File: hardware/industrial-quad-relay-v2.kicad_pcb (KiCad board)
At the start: 2 copper layers, 40 x 40 mm, 36 parts, among them P1 CON-SENSOR, P2 Digital Output, P3 Debug, P4 Boot, U1 XMC1100, U2 CPC1020N, U3 CPC1020N, U4 CPC1020N, U5 CPC1020N, U6 DRILL, U7 DRILL, U8 DRILL, U9 DRILL

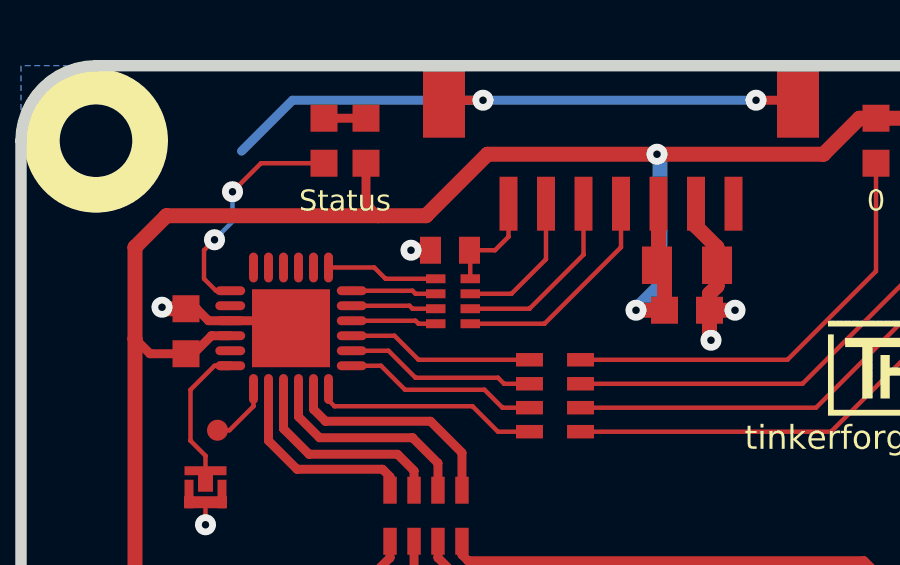
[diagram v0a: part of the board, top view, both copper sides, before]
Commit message: Change capacitor footprint(s) to C0402F
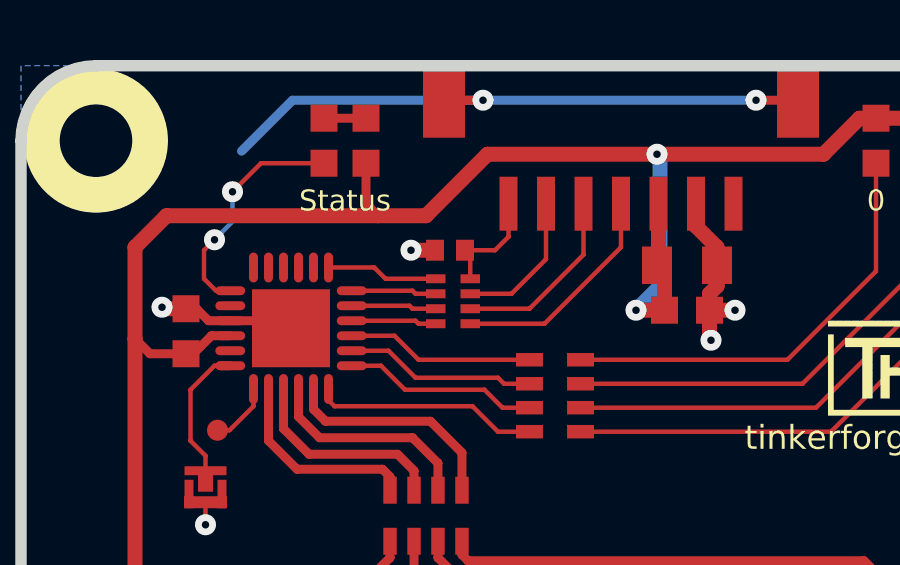
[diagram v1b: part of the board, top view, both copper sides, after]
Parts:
- C1, C4: footprint C0603F -> kicad-libraries:C0603F
- C2: footprint C0402E -> kicad-libraries:C0402F
- C3: footprint C0805 -> kicad-libraries:C0805
- D1, D2, D3, D4, D5: footprint D0603F -> kicad-libraries:D0603F
- P1: footprint CON-SENSOR2 -> kicad-libraries:CON-SENSOR2
- P2: footprint OQ_8P -> kicad-libraries:OQ_8P
- R1, R2, R3, R4: footprint R1210 -> kicad-libraries:R1210
- R5: footprint R0603F -> kicad-libraries:R0603F
- RP1, RP3: footprint 0603X4 -> kicad-libraries:0603X4
- U2, U3, U4, U5: footprint SOP4-WIDE -> kicad-libraries:SOP4-WIDE
- U6, U7, U8, U9: footprint DRILL_NP -> kicad-libraries:DRILL_NP
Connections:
- P1 pad 1: (no net) -> Net-(P1-Pad1)
- U1 pad 11: (no net) -> Net-(U1-Pad11)
- U1 pad 2: (no net) -> Net-(U1-Pad2)
- U1 pad 3: (no net) -> Net-(U1-Pad3)
- U1 pad 4: (no net) -> Net-(U1-Pad4)
- U1 pad 5: (no net) -> Net-(U1-Pad5)
- U1 pad 6: (no net) -> Net-(U1-Pad6)
- U1 pad 8: (no net) -> Net-(U1-Pad8)
